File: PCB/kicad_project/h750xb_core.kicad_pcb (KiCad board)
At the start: 6 copper layers, 50 x 50 mm, 97 parts, among them Q1 Q_NMOS_GSD, SW1 SW_DPST, SW2 SW_DPST, U1 STM32H750XBHx, U2 TPS74801DRC, U3 TPS82130, U4 REF3020, U7 W25Q32JVZP, U8 W25Q32JVZP, Y1 32M, Y2 32.768k

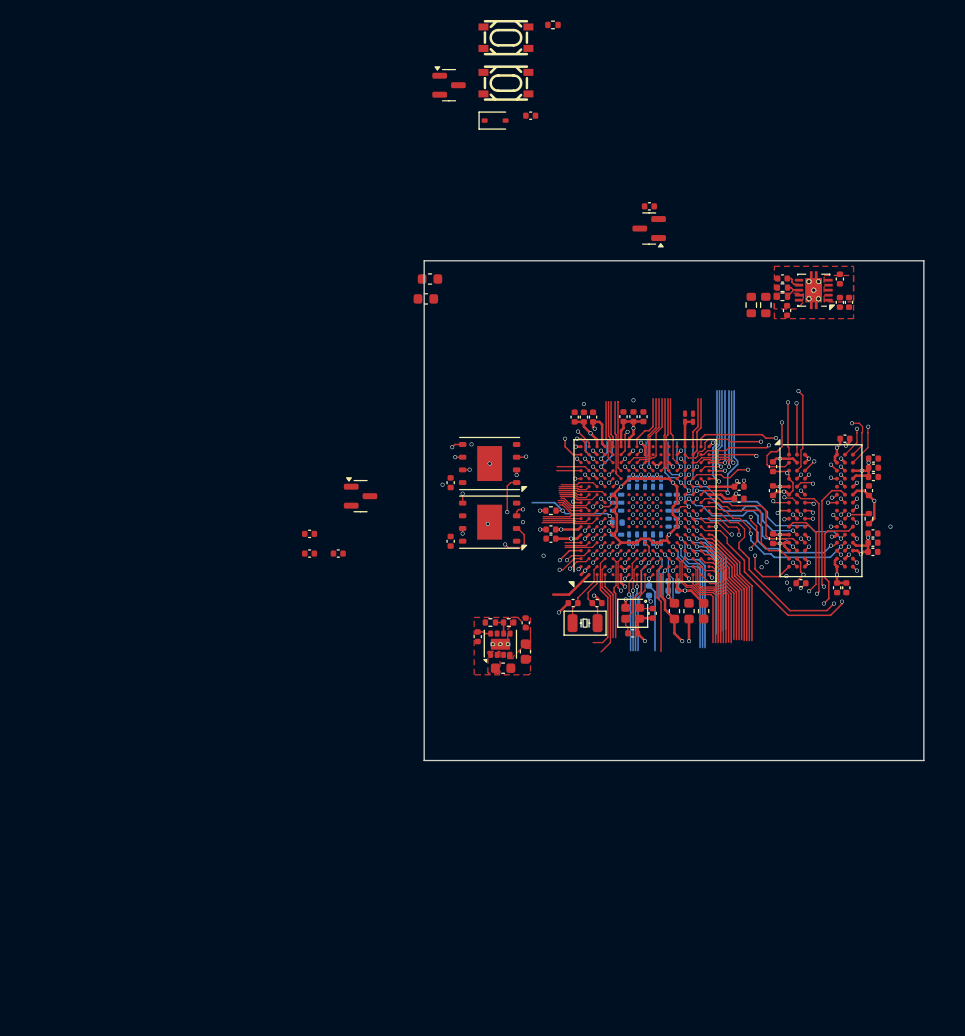
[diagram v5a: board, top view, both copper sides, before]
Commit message: 铺铜，增加BTB
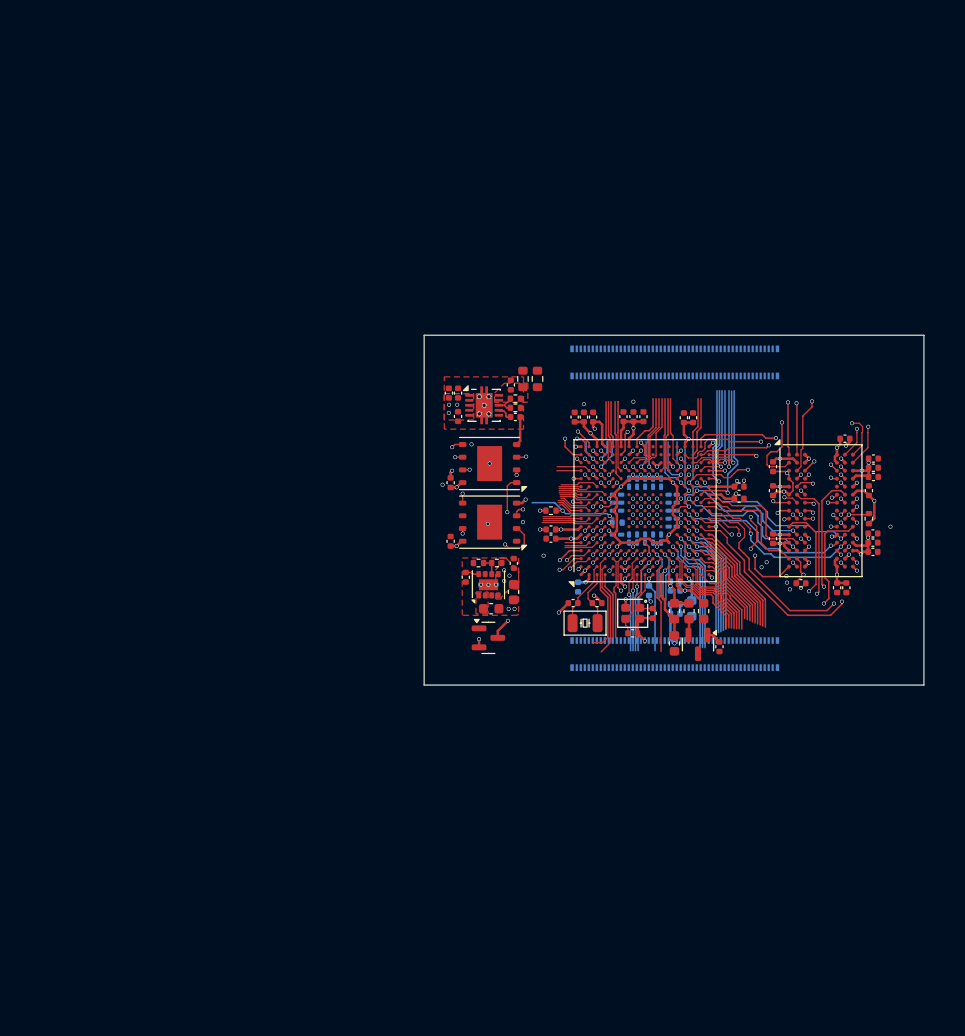
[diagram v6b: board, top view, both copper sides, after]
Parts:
- removed C46: 100nF, Capacitor_SMD:C_0402_1005Metric
- removed D1: D, Diode_SMD:D_SOD-323
- removed Q1: Q_NMOS_GSD, Package_TO_SOT_SMD:SOT-23
- removed R3: 47kΩ, Resistor_SMD:R_0402_1005Metric
- removed SW1, SW2: SW_DPST, my:SW_SMD_4P-L4.2-W3.2-P2.15-LS4.6-1
- added REF**: HIROSE_DF40C-100DP-0.4V_51_, HRS:HIROSE_DF40C-100DP-0.4V_51_, B.Cu at (40.3, 79.4)
- added REF**: HIROSE_DF40C-100DP-0.4V_51_, HRS:HIROSE_DF40C-100DP-0.4V_51_, B.Cu at (40.3, 108.6)
- C16, C2: footprint Capacitor_SMD:C_0201_0603Metric_Pad0.64x0.40mm_HandSolder -> Capacitor_SMD:C_0402_1005Metric
- C25, C26, C37, FB3: moved to B.Cu
- C36: value 4.7uF -> 0.47uF
- moved C36 56.4 mm to (44.8, 107.9), turned to -90 degrees
- moved FB4 42.5 mm to (40.3, 107.5), turned to 90 degrees
- moved FB3 42.1 mm to (42.0, 104.0), turned to -90 degrees
- moved U4 41.9 mm to (42.7, 107.6), turned to -90 degrees
- moved C38 41.1 mm to (17.7, 82.5), turned to 90 degrees
- moved C41 40.6 mm to (18.7, 84.8), turned to 90 degrees
- moved C39 39.3 mm to (18.7, 82.5), turned to 90 degrees
- moved C25 37.5 mm to (40.4, 104.6)
- moved C26 36.9 mm to (40.4, 103.6)
- moved U2 34.9 mm to (21.3, 83.7), turned to 0 degrees
- moved C40 30.1 mm to (24.4, 84.9), turned to 0 degrees
- moved R8 29.3 mm to (24.4, 84.0), turned to 180 degrees
- moved C42 28.6 mm to (23.9, 81.7), turned to -90 degrees
- moved R7 28.6 mm to (24.4, 83.0), turned to 0 degrees
- moved R4 25.4 mm to (25.2, 81.1), turned to 90 degrees
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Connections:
- net /VBAT renamed /ex_VBAT
- C36 pad 1: /mcu/BOOT0 -> +3V3
- U1 pad E16: /mcu/USB_FS_D+ -> unconnected-(U1-PA12-PadE16)
- U1 pad E17: /mcu/USB_FS_D- -> unconnected-(U1-PA11-PadE17)
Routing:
- net /mcu/VDDLDO: track 9.87 -> 43.8 mm
- net /mcu/VCAP: track 10.0 -> 39.2 mm
- net /mcu/VBAT: track 4.43 -> 13.2 mm, vias 0 -> 2
- net +3V3: track 71.5 -> 77.0 mm, vias 28 -> 38
- net unconnected-(U1-PA12-PadE16): track 0.00 -> 5.49 mm
- net /mcu/USB_FS_D+: track 5.49 -> 0.00 mm
- net GND: track 39.0 -> 43.8 mm, vias 59 -> 63
- net unconnected-(U1-PA11-PadE17): track 0.00 -> 4.58 mm
- net /mcu/USB_FS_D-: track 4.58 -> 0.00 mm
- net /mcu/VSSA: track 0.57 -> 5.15 mm
- net /mcu/VDDA: track 7.53 -> 11.5 mm
- net unconnected-(U1-PA3-PadU2): track 8.71 -> 6.87 mm
- net /mcu/SDRAM_D26: track 34.2 -> 35.8 mm
- net unconnected-(U1-PA5-PadT3): track 9.92 -> 8.49 mm
- net unconnected-(U1-PA4-PadU3): track 9.44 -> 8.11 mm
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- added copper zone on In4.Cu, net +3V3
- added copper zone on In1.Cu, net GND
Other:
- board size 50 x 50 mm -> 50 x 35 mm

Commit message: 收尾
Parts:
- removed REF**: HIROSE_DF40C-100DP-0.4V_51_, HRS:HIROSE_DF40C-100DP-0.4V_51_
- added J1: DF40C-100DP-0.4V_51_, HRS:HIROSE_DF40C-100DP-0.4V_51_, B.Cu at (40.3, 80.4)
- J2: renamed from REF**; value HIROSE_DF40C-100DP-0.4V_51_ -> DF40C-100DP-0.4V_51_
- moved R4 1.11 mm to (25.7, 82.0), turned to 0 degrees
- moved R11 0.99 mm to (25.7, 80.7), turned to 0 degrees
- moved J2 0.51 mm to (40.3, 108.1)
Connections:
- J2 pad 1: (no net) -> unconnected-(J2-Pad1)
- J2 pad 10: (no net) -> unconnected-(J2-Pad10)
- J2 pad 100: (no net) -> unconnected-(J2-Pad100)
- J2 pad 11: (no net) -> unconnected-(J2-Pad11)
- J2 pad 12: (no net) -> unconnected-(J2-Pad12)
- J2 pad 13: (no net) -> unconnected-(J2-Pad13)
- J2 pad 14: (no net) -> unconnected-(J2-Pad14)
- J2 pad 15: (no net) -> unconnected-(J2-Pad15)
- J2 pad 16: (no net) -> unconnected-(J2-Pad16)
- J2 pad 17: (no net) -> unconnected-(J2-Pad17)
- J2 pad 18: (no net) -> unconnected-(J2-Pad18)
- J2 pad 19: (no net) -> unconnected-(J2-Pad19)
- J2 pad 2: (no net) -> unconnected-(J2-Pad2)
- J2 pad 20: (no net) -> unconnected-(J2-Pad20)
- J2 pad 21: (no net) -> unconnected-(J2-Pad21)
- J2 pad 22: (no net) -> unconnected-(J2-Pad22)
- J2 pad 23: (no net) -> unconnected-(J2-Pad23)
- J2 pad 24: (no net) -> unconnected-(J2-Pad24)
- J2 pad 25: (no net) -> unconnected-(J2-Pad25)
- J2 pad 26: (no net) -> unconnected-(J2-Pad26)
- J2 pad 27: (no net) -> unconnected-(J2-Pad27)
- J2 pad 28: (no net) -> unconnected-(J2-Pad28)
- J2 pad 29: (no net) -> unconnected-(J2-Pad29)
- J2 pad 3: (no net) -> unconnected-(J2-Pad3)
- J2 pad 30: (no net) -> unconnected-(J2-Pad30)
- J2 pad 31: (no net) -> unconnected-(J2-Pad31)
- J2 pad 32: (no net) -> unconnected-(J2-Pad32)
- J2 pad 33: (no net) -> unconnected-(J2-Pad33)
- J2 pad 34: (no net) -> unconnected-(J2-Pad34)
- J2 pad 35: (no net) -> unconnected-(J2-Pad35)
- J2 pad 36: (no net) -> unconnected-(J2-Pad36)
- J2 pad 37: (no net) -> unconnected-(J2-Pad37)
- J2 pad 38: (no net) -> unconnected-(J2-Pad38)
- J2 pad 39: (no net) -> unconnected-(J2-Pad39)
- J2 pad 4: (no net) -> unconnected-(J2-Pad4)
- J2 pad 40: (no net) -> unconnected-(J2-Pad40)
- J2 pad 41: (no net) -> unconnected-(J2-Pad41)
- J2 pad 42: (no net) -> unconnected-(J2-Pad42)
- J2 pad 43: (no net) -> unconnected-(J2-Pad43)
- J2 pad 44: (no net) -> unconnected-(J2-Pad44)
- J2 pad 45: (no net) -> unconnected-(J2-Pad45)
- J2 pad 46: (no net) -> unconnected-(J2-Pad46)
- J2 pad 47: (no net) -> unconnected-(J2-Pad47)
- J2 pad 48: (no net) -> unconnected-(J2-Pad48)
- J2 pad 49: (no net) -> unconnected-(J2-Pad49)
- J2 pad 5: (no net) -> unconnected-(J2-Pad5)
- J2 pad 50: (no net) -> unconnected-(J2-Pad50)
- J2 pad 51: (no net) -> unconnected-(J2-Pad51)
- J2 pad 52: (no net) -> unconnected-(J2-Pad52)
- J2 pad 53: (no net) -> unconnected-(J2-Pad53)
- J2 pad 54: (no net) -> unconnected-(J2-Pad54)
- J2 pad 55: (no net) -> unconnected-(J2-Pad55)
- J2 pad 56: (no net) -> unconnected-(J2-Pad56)
- J2 pad 57: (no net) -> unconnected-(J2-Pad57)
- J2 pad 58: (no net) -> unconnected-(J2-Pad58)
- J2 pad 59: (no net) -> unconnected-(J2-Pad59)
- J2 pad 6: (no net) -> unconnected-(J2-Pad6)
- J2 pad 60: (no net) -> unconnected-(J2-Pad60)
- J2 pad 61: (no net) -> unconnected-(J2-Pad61)
- J2 pad 62: (no net) -> unconnected-(J2-Pad62)
- J2 pad 63: (no net) -> unconnected-(J2-Pad63)
- J2 pad 64: (no net) -> unconnected-(J2-Pad64)
- J2 pad 65: (no net) -> unconnected-(J2-Pad65)
- J2 pad 66: (no net) -> unconnected-(J2-Pad66)
- J2 pad 67: (no net) -> unconnected-(J2-Pad67)
- J2 pad 68: (no net) -> unconnected-(J2-Pad68)
- J2 pad 69: (no net) -> unconnected-(J2-Pad69)
- J2 pad 7: (no net) -> unconnected-(J2-Pad7)
- J2 pad 70: (no net) -> unconnected-(J2-Pad70)
- J2 pad 71: (no net) -> unconnected-(J2-Pad71)
- J2 pad 72: (no net) -> unconnected-(J2-Pad72)
- J2 pad 73: (no net) -> unconnected-(J2-Pad73)
- J2 pad 74: (no net) -> unconnected-(J2-Pad74)
- J2 pad 75: (no net) -> unconnected-(J2-Pad75)
- J2 pad 76: (no net) -> unconnected-(J2-Pad76)
- J2 pad 77: (no net) -> unconnected-(J2-Pad77)
- J2 pad 78: (no net) -> unconnected-(J2-Pad78)
- J2 pad 79: (no net) -> unconnected-(J2-Pad79)
- J2 pad 8: (no net) -> unconnected-(J2-Pad8)
- J2 pad 80: (no net) -> unconnected-(J2-Pad80)
- J2 pad 81: (no net) -> unconnected-(J2-Pad81)
- J2 pad 82: (no net) -> unconnected-(J2-Pad82)
- J2 pad 83: (no net) -> unconnected-(J2-Pad83)
- J2 pad 84: (no net) -> unconnected-(J2-Pad84)
- J2 pad 85: (no net) -> unconnected-(J2-Pad85)
- J2 pad 86: (no net) -> unconnected-(J2-Pad86)
- J2 pad 87: (no net) -> unconnected-(J2-Pad87)
- J2 pad 88: (no net) -> unconnected-(J2-Pad88)
- J2 pad 89: (no net) -> unconnected-(J2-Pad89)
- J2 pad 9: (no net) -> unconnected-(J2-Pad9)
- J2 pad 90: (no net) -> unconnected-(J2-Pad90)
- J2 pad 91: (no net) -> unconnected-(J2-Pad91)
- J2 pad 92: (no net) -> unconnected-(J2-Pad92)
- J2 pad 93: (no net) -> unconnected-(J2-Pad93)
- J2 pad 94: (no net) -> unconnected-(J2-Pad94)
- J2 pad 95: (no net) -> unconnected-(J2-Pad95)
- J2 pad 96: (no net) -> unconnected-(J2-Pad96)
- J2 pad 97: (no net) -> unconnected-(J2-Pad97)
- J2 pad 98: (no net) -> unconnected-(J2-Pad98)
- J2 pad 99: (no net) -> unconnected-(J2-Pad99)
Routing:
- net GND: track 43.8 -> 80.3 mm
- net unconnected-(U1-PJ14-PadD10): track 0.57 -> 17.1 mm
- net unconnected-(U1-PJ13-PadE10): track 1.37 -> 16.7 mm
- net unconnected-(U1-PK7-PadD7): track 0.57 -> 13.6 mm
- net unconnected-(U1-PB4-PadB7): track 0.57 -> 10.9 mm
- net unconnected-(U1-PK6-PadC7): track 0.57 -> 10.2 mm
- net /mcu/VCAP: track 39.2 -> 48.6 mm, vias 3 -> 5
- net unconnected-(U1-PB3-PadC6): track 0.57 -> 9.40 mm
- net +3V3: track 77.0 -> 84.0 mm, vias 38 -> 39
- net /mcu/BOOT0: track 9.42 -> 16.3 mm
- net unconnected-(U1-PD2-PadD12): track 0.57 -> 6.89 mm
- net unconnected-(U1-PI13-PadH2): track 8.57 -> 2.57 mm
- net /mcu/NRST: track 8.01 -> 2.13 mm
- net /mcu/VDDLDO: track 43.8 -> 49.5 mm, vias 3 -> 5
- net unconnected-(U1-PB8-PadD5): track 0.57 -> 6.08 mm
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- added copper zone on B.Cu, net +3V3
- added copper zone on B.Cu, net GND
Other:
- rule pad_to_mask_clearance: 0.038 -> 0
